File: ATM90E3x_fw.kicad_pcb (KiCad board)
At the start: 2 copper layers, 50.8 x 50.8 mm, 81 parts, among them IC1 ATM90E36_ATM90E36, J1 CONN_01X04, J10 GROVE-SMD-90D, J11 CONN_01X03, J2 GS3, J3 CONN_01X06, J4 CONN_01X04, J5 RJ45, J6 GS3, J7 GS3, J8 CONN_01X06, J9 GS3, U1 ROF-78E, Y1 Crystal_GND24

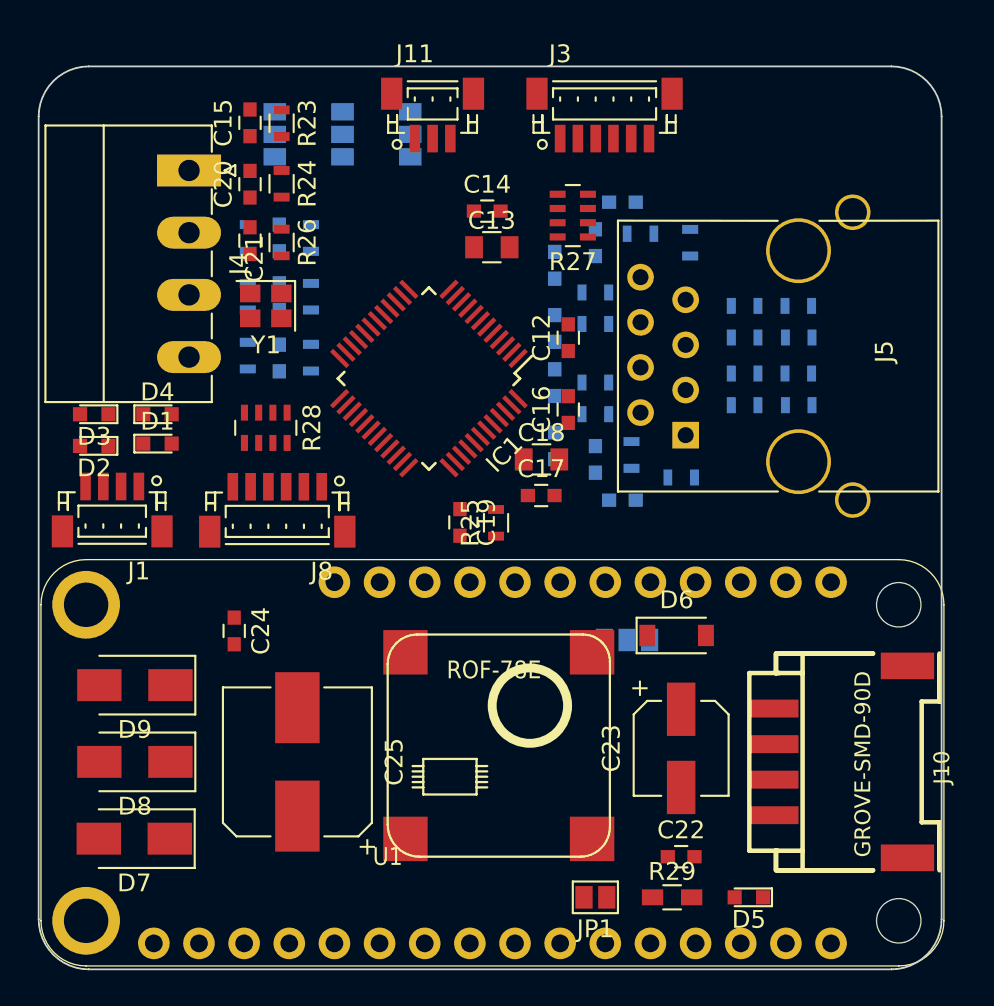
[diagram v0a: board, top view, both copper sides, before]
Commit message: Partial autoroute
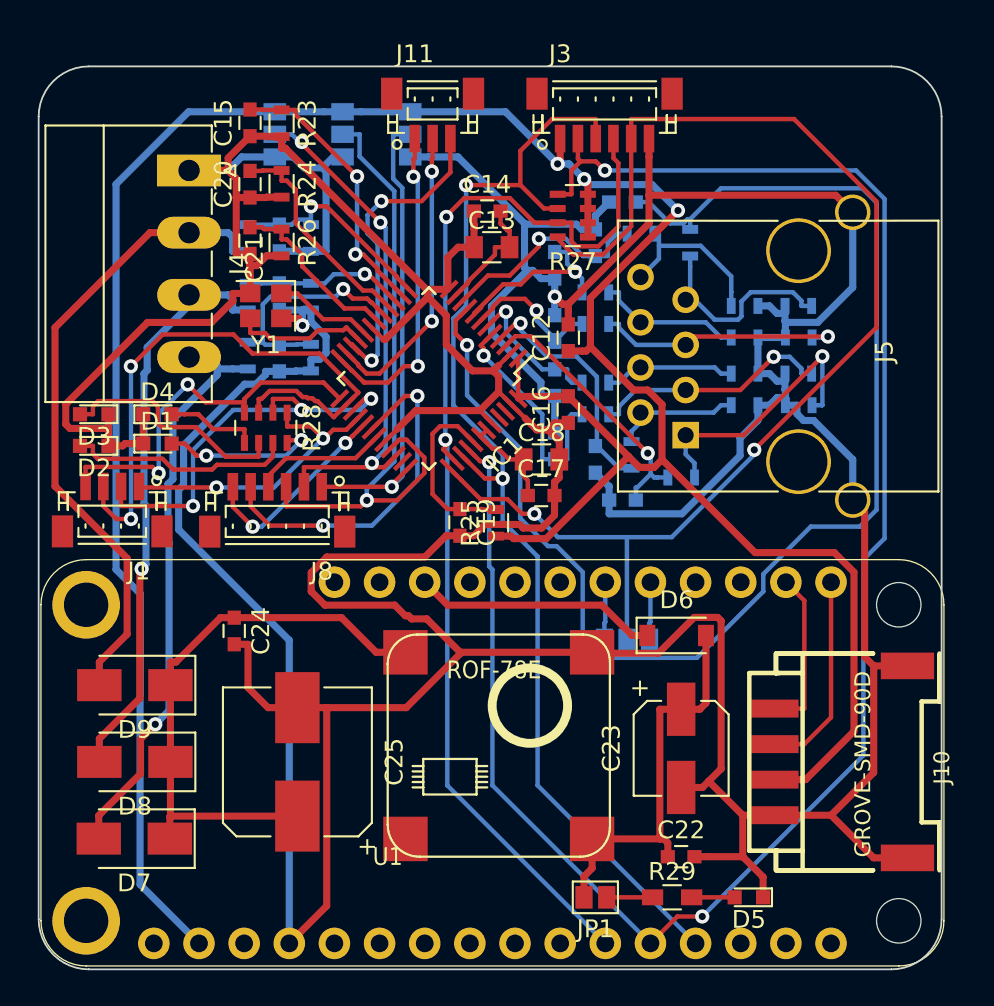
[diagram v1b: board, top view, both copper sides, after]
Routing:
- net GND: track 0.00 -> 385.0 mm, vias 0 -> 2
- net VDD: track 0.00 -> 154.2 mm, vias 0 -> 3
- net MOSI: track 0.00 -> 102.7 mm, vias 0 -> 3
- net IP: track 0.00 -> 76.5 mm, vias 0 -> 1
- net CS: track 0.00 -> 70.6 mm, vias 0 -> 2
- net MISO: track 0.00 -> 65.2 mm, vias 0 -> 2
- net SCLK: track 0.00 -> 63.6 mm, vias 0 -> 2
- net UC: track 0.00 -> 36.4 mm
- net PM0: track 0.00 -> 36.1 mm, vias 0 -> 1
- net CF2: track 0.00 -> 34.2 mm, vias 0 -> 2
- net UA: track 0.00 -> 32.9 mm, vias 0 -> 1
- net UB: track 0.00 -> 32.7 mm, vias 0 -> 1
- net /Featherwing/VIN: track 0.00 -> 32.2 mm
- net PM1: track 0.00 -> 28.9 mm, vias 0 -> 3
- net DMA: track 0.00 -> 26.7 mm, vias 0 -> 1
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
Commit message: Complete autoroute
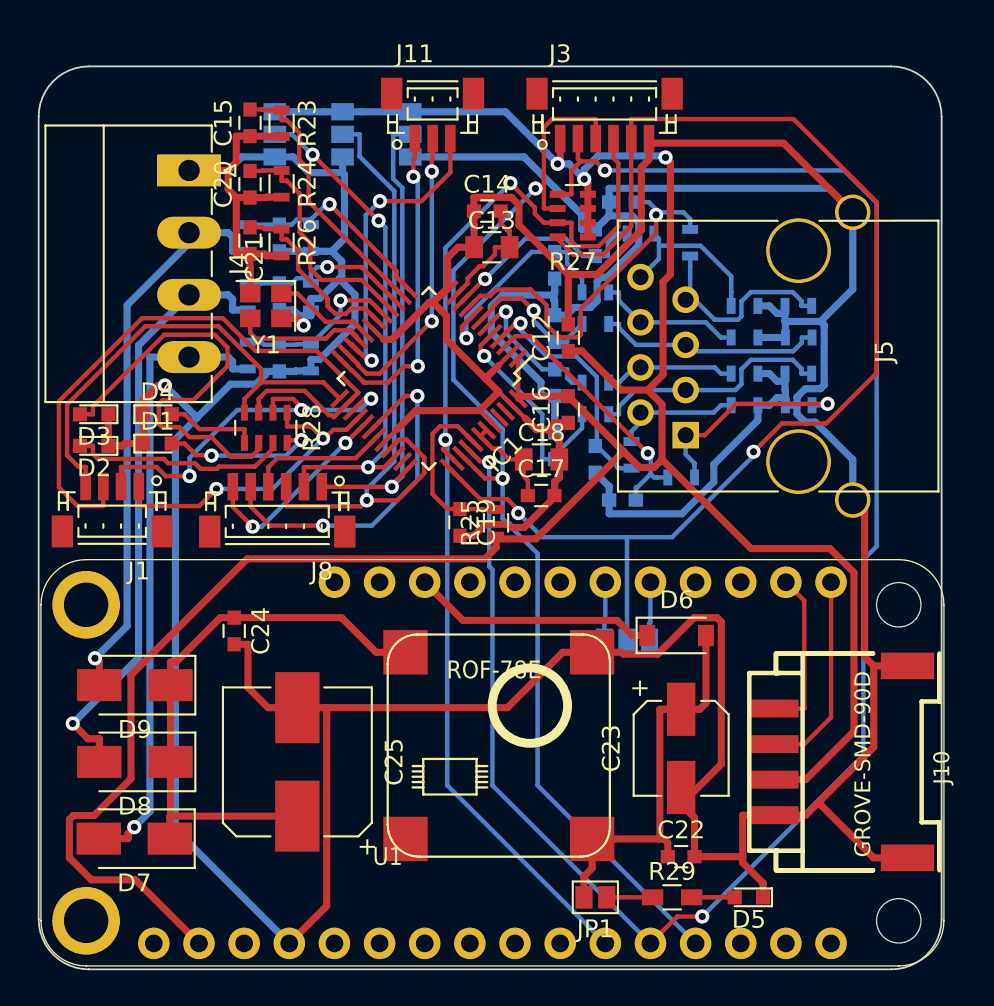
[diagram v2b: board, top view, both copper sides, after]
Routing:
- net IP: track 76.5 -> 21.3 mm
- net Net-(D3-Pad2): track 13.2 -> 24.5 mm
- net VDD: track 154.2 -> 147.9 mm
- net CF1: track 21.5 -> 26.7 mm, vias 2 -> 0
- net UC: track 36.4 -> 32.2 mm, vias 0 -> 1
- net V3P: track 13.5 -> 9.53 mm
- net I1P_IN: track 15.4 -> 12.2 mm
- net CF2: track 34.2 -> 37.1 mm, vias 2 -> 0
- net I3N: track 10.0 -> 12.7 mm
- net UA: track 32.9 -> 35.3 mm
- net MISO: track 65.2 -> 62.9 mm
- net CF3: track 23.6 -> 21.9 mm
- net CS: track 70.6 -> 72.2 mm
- net CF4: track 17.1 -> 18.6 mm
- net I3P_IN: track 14.1 -> 12.7 mm, vias 1 -> 0
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
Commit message: And bottom ground place
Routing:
- added copper zone on B.Cu, net GND
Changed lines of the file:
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@@
   (segment (start 135.8767 59.436) (end 135.8625 59.4502) (width 0.4) (layer F.Cu) (net 84))
   (segment (start 133.8495 59.4502) (end 133.8315 59.4322) (width 0.4) (layer F.Cu) (net 84))
+  (zone (net 49) (net_name GND) (layer B.Cu) (hatch edge 0.508)
+    (connect_pads (clearance 0.508))
+    (min_thickness 0.254)
+    (fill yes (arc_segments 16) (thermal_gap 0.508) (thermal_bridge_width 0.508))
+    (polygon
+      (pts
+        (xy 106.68 40.64) (xy 157.48 40.64) (xy 157.48 91.44) (xy 106.68 91.44)
+      )
+    )
+  )
 )

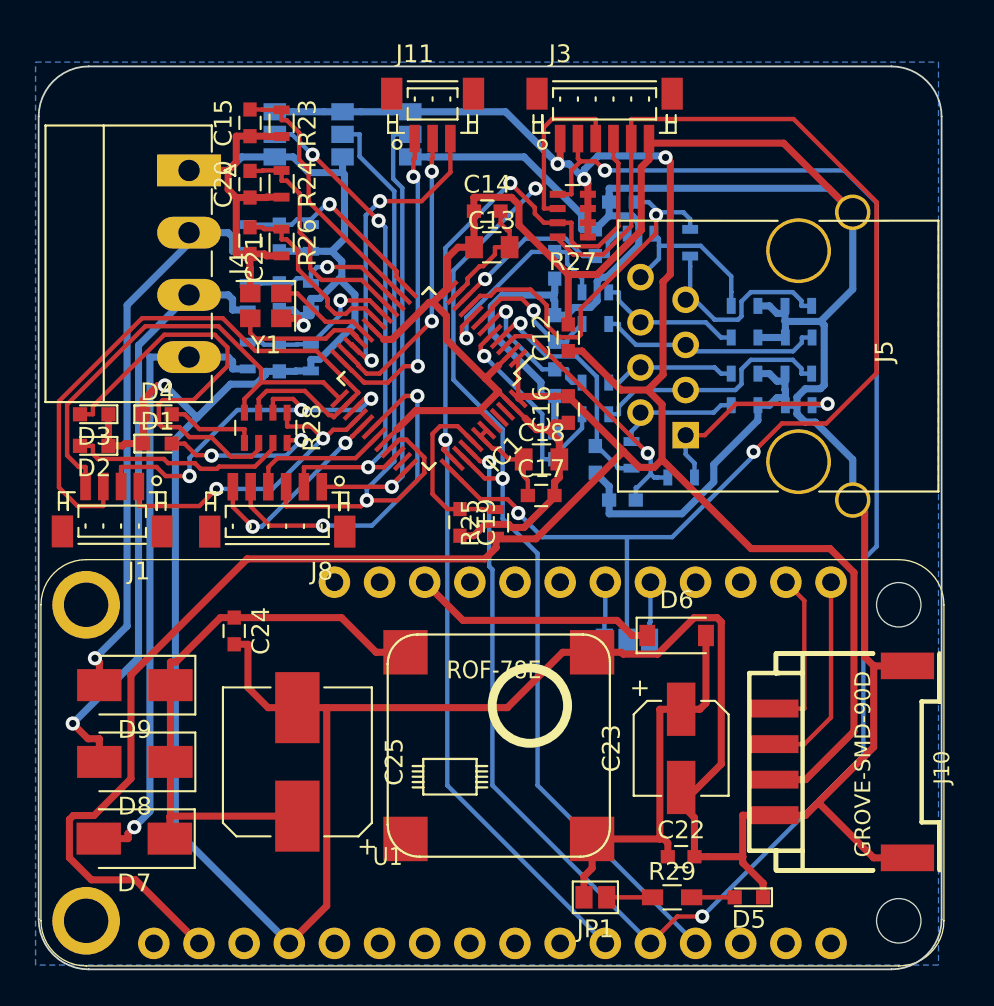
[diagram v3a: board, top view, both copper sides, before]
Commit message: Neaten up silkscreen
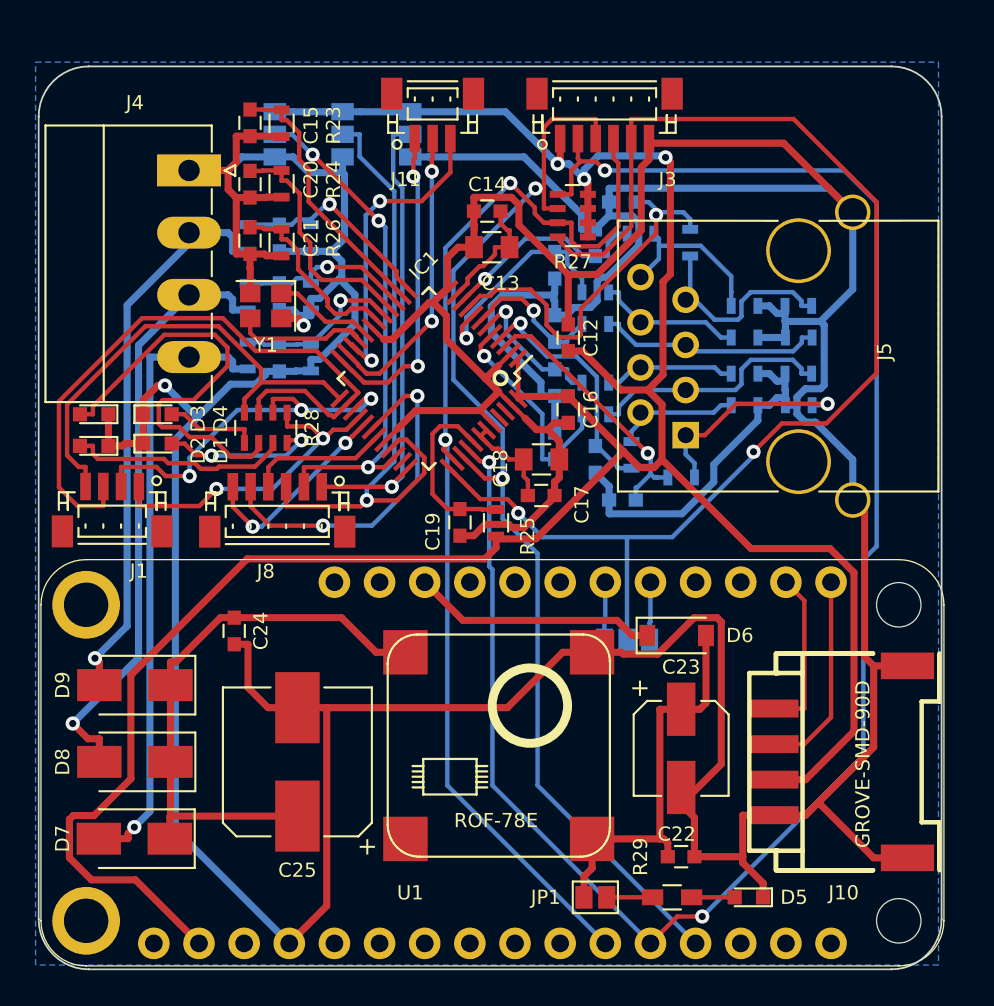
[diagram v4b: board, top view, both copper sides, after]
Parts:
- moved LOGO1 25.4 mm to (114.8, 79.2), turned to 270 degrees
- moved LOGO2 10.7 mm to (122.2, 79.0), turned to 270 degrees
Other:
- board text added: "ATM90E3X Featherwing v1.0 30/07/2017 Design by: Tisham Dhar http://whatnick.com (CS pins - 9 or 10)"

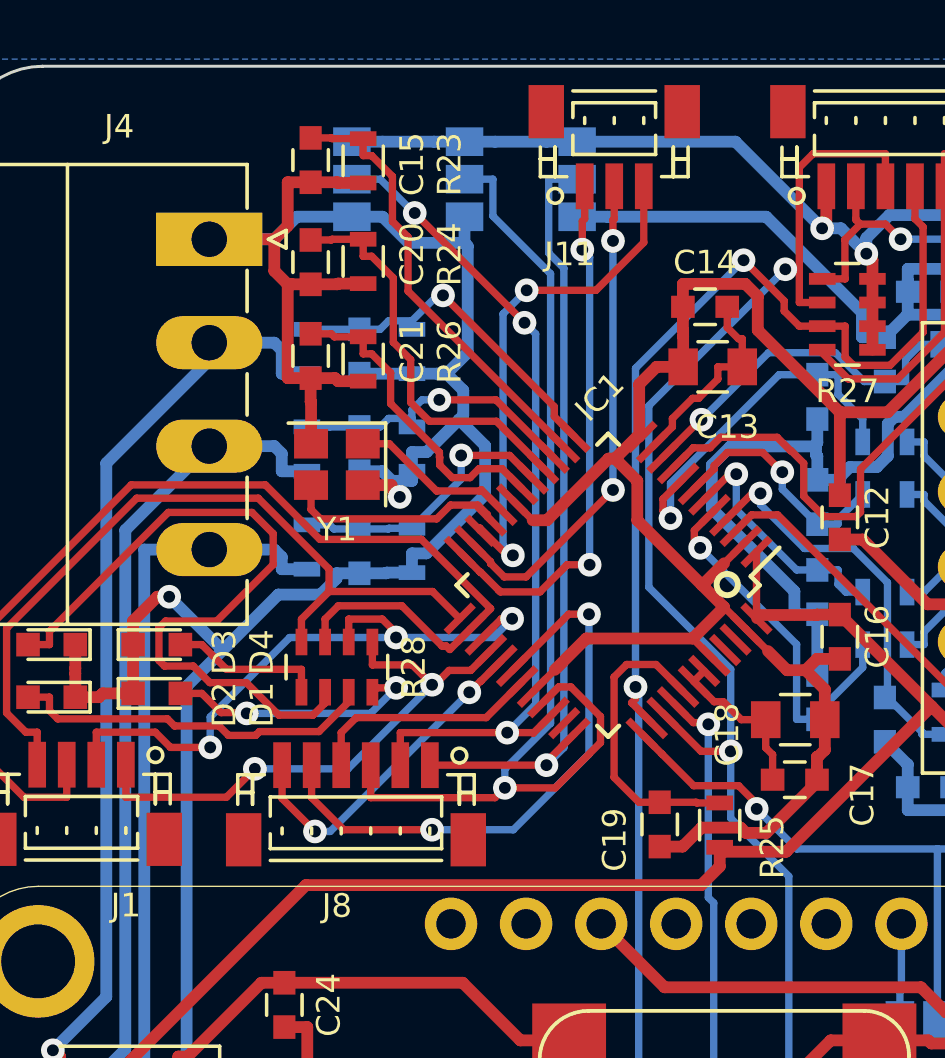
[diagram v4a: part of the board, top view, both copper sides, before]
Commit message: Neaten up silkscreen
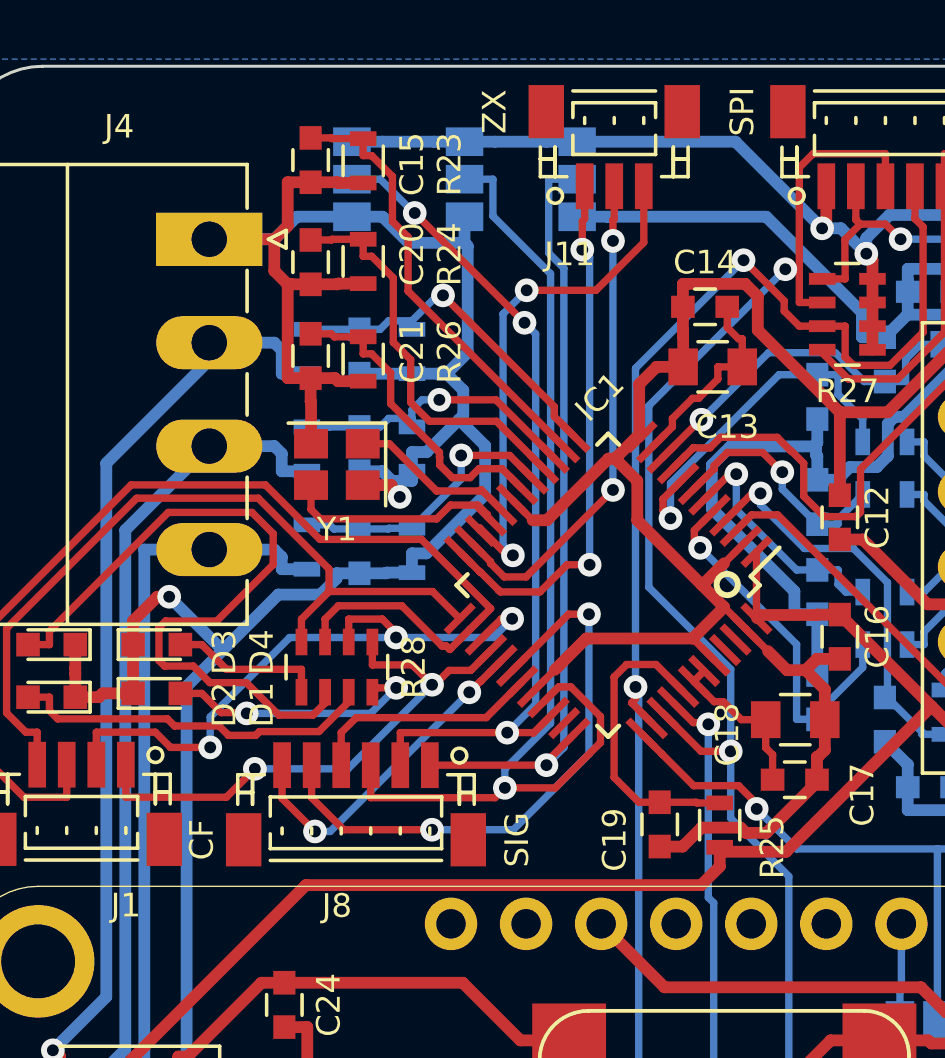
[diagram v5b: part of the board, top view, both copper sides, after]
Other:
- board text added: "CF"
- board text added: "CS"
- board text added: "DMA"
- board text added: "PM0"
- board text added: "PM1"
- board text added: "SIG"
- board text added: "SPI"
- board text added: "ZX"
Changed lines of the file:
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@@
     (area 105.49 40.64 157.985001 91.9408)
     (thickness 1.6)
-    (drawings 11)
+    (drawings 19)
     (tracks 1003)
     (zones 0)
@@
     (35 F.Paste user hide)
     (36 B.SilkS user)
-    (37 F.SilkS user hide)
+    (37 F.SilkS user)
     (38 B.Mask user hide)
     (39 F.Mask user hide)
@@
     (44 Edge.Cuts user)
     (45 Margin user hide)
-    (46 B.CrtYd user)
-    (47 F.CrtYd user hide)
+    (46 B.CrtYd user hide)
+    (47 F.CrtYd user)
     (48 B.Fab user hide)
     (49 F.Fab user hide)
@@
     )
   )
+  (gr_text CF (at 115.062 67.056 90) (layer F.SilkS)
+    (effects (font (size 0.8 0.8) (thickness 0.2)))
+  )
+  (gr_text SIG (at 125.73 67.056 90) (layer F.SilkS)
+    (effects (font (size 0.8 0.8) (thickness 0.2)))
+  )
+  (gr_text ZX (at 124.968 42.418 90) (layer F.SilkS)
+    (effects (font (size 0.8 0.8) (thickness 0.2)))
+  )
+  (gr_text SPI (at 133.35 42.418 90) (layer F.SilkS)
+    (effects (font (size 0.8 0.8) (thickness 0.2)))
+  )
+  (gr_text DMA (at 127.762 47.752) (layer B.SilkS)
+    (effects (font (size 0.8 0.8) (thickness 0.2)) (justify mirror))
+  )
+  (gr_text PM1 (at 123.952 47.752) (layer B.SilkS)
+    (effects (font (size 0.8 0.8) (thickness 0.2)) (justify mirror))
+  )
+  (gr_text PM0 (at 120.142 47.752) (layer B.SilkS)
+    (effects (font (size 0.8 0.8) (thickness 0.2)) (justify mirror))
+  )
+  (gr_text CS (at 139.954 75.184) (layer B.SilkS)
+    (effects (font (size 0.8 0.8) (thickness 0.2)) (justify mirror))
+  )
   (gr_text "ATM90E3X Featherwing\nv1.0 30/07/2017\nDesign by: Tisham Dhar\nhttp://whatnick.com\n(CS pins - 9 or 10)" (at 140.462 81.534) (layer B.SilkS)
